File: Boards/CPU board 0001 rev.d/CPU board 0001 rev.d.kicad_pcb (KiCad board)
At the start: 2 copper layers, 165.9 x 187.4 mm, 78 parts, among them J1 CEC card edge connector large, U1 SPARE, U10 7432, U11 7442, U12 7406, U13 7406, U14 7442, U15 7442, U16 M8216, U17 M8216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

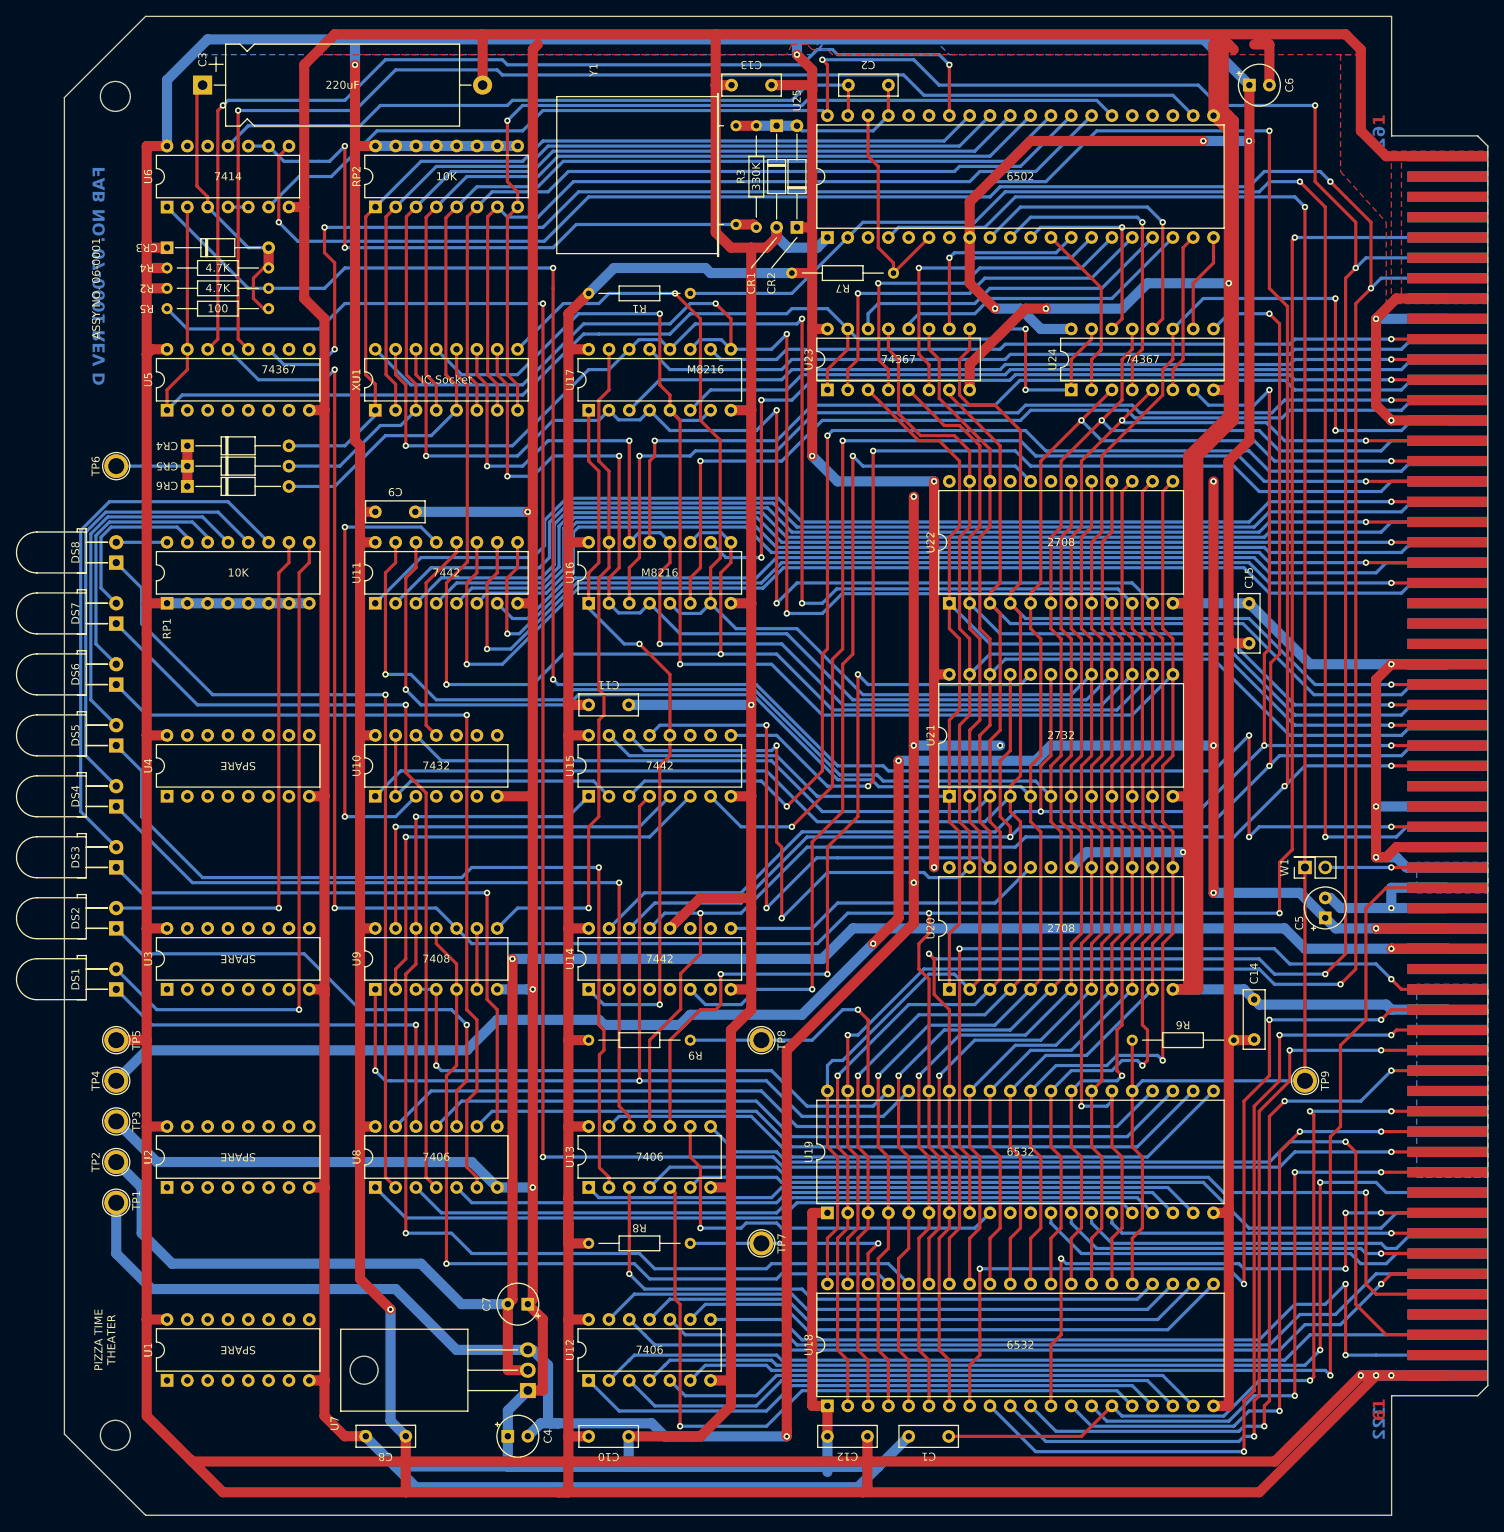
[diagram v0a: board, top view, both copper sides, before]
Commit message: updated boards per real one
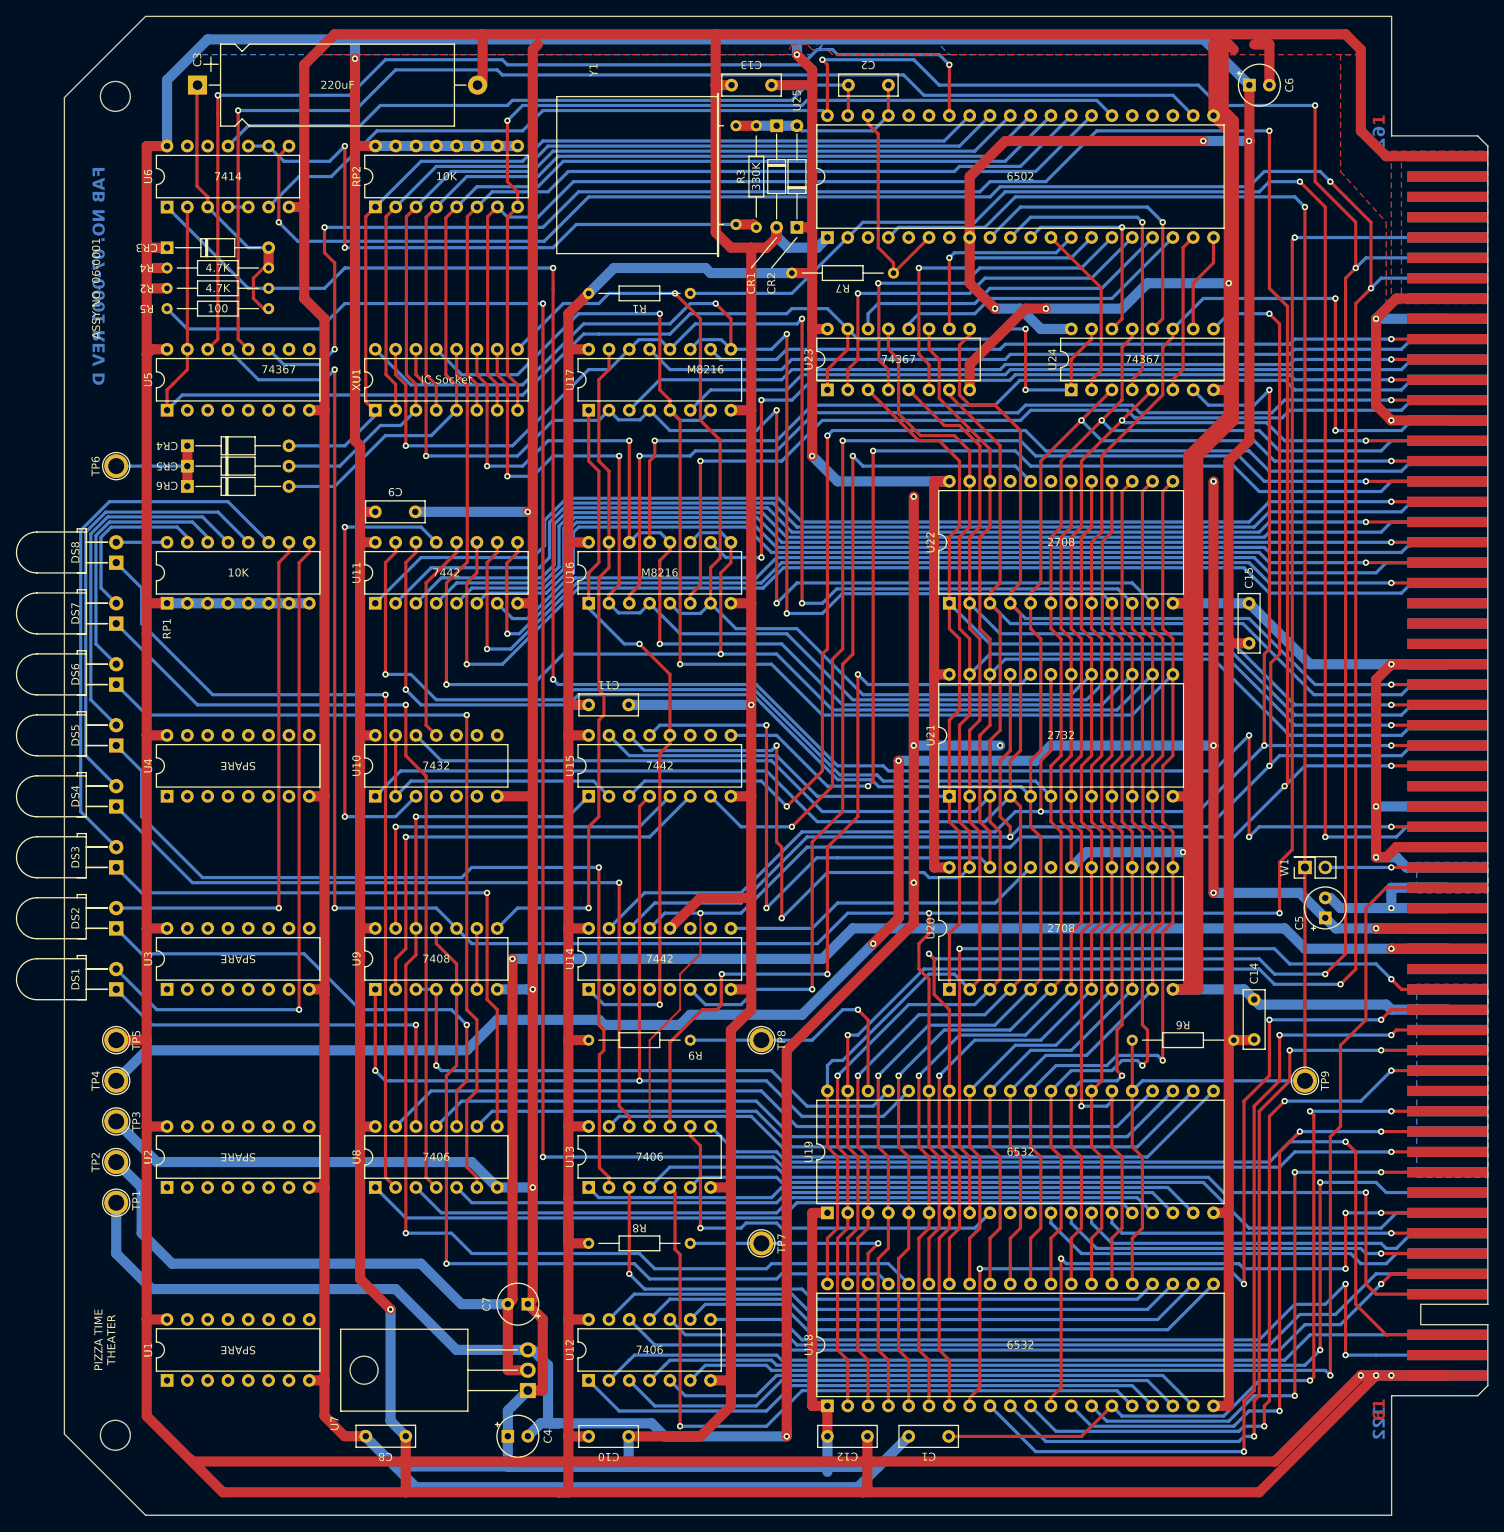
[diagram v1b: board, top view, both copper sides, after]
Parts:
- moved C3 0.63 mm to (58.4, 19.1)
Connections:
- U20 pad 24: unconnected-(U20-VCC-Pad24) -> +5V
- U22 pad 24: unconnected-(U22-VCC-Pad24) -> +5V
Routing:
- net +5V: track 1491.3 -> 1498.9 mm, vias 12 -> 10
- net cpu R/~{W}: track 132.6 -> 133.7 mm
- net Net-(CR3-A): track 35.8 -> 34.8 mm

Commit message: sent off boards for manufacture
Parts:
- U20, U22: value 2708 -> UNUSED
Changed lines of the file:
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@@
         (effects (font (size 1 1) (thickness 0.15)))
     )
-    (fp_text value "2708" (at 7.62 13.97 180) (layer "F.SilkS")
+    (fp_text value "UNUSED" (at 7.62 13.97 180) (layer "F.SilkS")
         (effects (font (size 1 1) (thickness 0.15)))
     )
@@
         (effects (font (size 1 1) (thickness 0.15)))
     )
-    (fp_text value "4.7K" (at 3.81 1.92) (layer "F.Fab")
+    (fp_text value "4.7K" (at 3.81 0) (layer "F.SilkS")
         (effects (font (size 1 1) (thickness 0.15)))
     )
@@
         (effects (font (size 1 1) (thickness 0.15)))
     )
-    (fp_text value "4.7K" (at 3.81 1.92) (layer "F.Fab")
+    (fp_text value "4.7K" (at 3.81 0) (layer "F.SilkS")
         (effects (font (size 1 1) (thickness 0.15)))
     )
@@
         (effects (font (size 1 1) (thickness 0.15)))
     )
-    (fp_text value "4.7K" (at 3.81 1.92) (layer "F.Fab")
+    (fp_text value "4.7K" (at 3.81 0) (layer "F.SilkS")
         (effects (font (size 1 1) (thickness 0.15)))
     )
@@
         (effects (font (size 1 1) (thickness 0.15)))
     )
-    (fp_text value "4.7K" (at 3.81 1.92) (layer "F.Fab")
+    (fp_text value "4.7K" (at 3.81 0) (layer "F.SilkS")
         (effects (font (size 1 1) (thickness 0.15)))
     )
@@
         (effects (font (size 1 1) (thickness 0.15)))
     )
-    (fp_text value "2708" (at 7.62 13.97 180) (layer "F.SilkS")
+    (fp_text value "UNUSED" (at 7.62 13.97 180) (layer "F.SilkS")
         (effects (font (size 1 1) (thickness 0.15)))
     )
@@
         (effects (font (size 1 1) (thickness 0.15)))
     )
-    (fp_text value "1Mhz" (at 17.16 4.6125) (layer "F.Fab")
+    (fp_text value "1Mhz" (at 5.715 12.065) (layer "F.SilkS")
         (effects (font (size 1 1) (thickness 0.15)))
     )
@@
         (effects (font (size 1 1) (thickness 0.15)))
     )
-    (fp_text value "4.7K" (at 3.81 1.92) (layer "F.Fab")
+    (fp_text value "4.7K" (at 3.81 0) (layer "F.SilkS")
         (effects (font (size 1 1) (thickness 0.15)))
     )

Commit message: revisions from real life boards
tip130a is actually tip30a, widened holes for crystal, widened holes for big power resistor, fixed cpu board LED resistors
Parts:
- RP1: value 10K -> 330
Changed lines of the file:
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@@
         (effects (font (size 1 1) (thickness 0.15)))
     )
-    (fp_text value "10K" (at 3.81 8.89 180) (layer "F.SilkS")
+    (fp_text value "330" (at 3.81 8.89 180) (layer "F.SilkS")
         (effects (font (size 1 1) (thickness 0.15)))
     )
@@
     (fp_line (start 16.135 2.5) (end -3.795 2.5)
       (stroke (width 0.1) (type solid)) (layer "F.Fab"))
-    (pad "1" thru_hole circle (at 0 0 270) (size 1.4 1.4) (drill 0.7) (layers "*.Cu" "*.Mask")
+    (pad "1" thru_hole circle (at 0 0 270) (size 2 2) (drill 1) (layers "*.Cu" "*.Mask")
       (net 8 "Net-(CR1-K)") (pinfunction "1") (pintype "passive"))
-    (pad "2" thru_hole circle (at 12.34 0 270) (size 1.4 1.4) (drill 0.7) (layers "*.Cu" "*.Mask")
+    (pad "2" thru_hole circle (at 12.34 0 270) (size 2 2) (drill 1) (layers "*.Cu" "*.Mask")
       (net 114 "Net-(R3-Pad1)") (pinfunction "2") (pintype "passive"))
     (model "${KICAD6_3DMODEL_DIR}/Crystal.3dshapes/Crystal_HC33-U_Horizontal.wrl"

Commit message: fixed rev.d pull up on CS and added render and schematic
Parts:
- added R10: 1K, Resistor_THT:R_Axial_DIN0309_L9.0mm_D3.2mm_P12.70mm_Horizontal, F.Cu at (151.1, 88.9)
- C1, C10, C11, C12, C13, C14, C15, C8, C9: footprint Capacitor_THT:C_Rect_L7.2mm_W2.5mm_P5.00mm_FKS2_FKP2_MKS2_MKP2 -> Capacitor_THT:C_Rect_L9.0mm_W2.5mm_P7.50mm_MKT
- CR1, CR2, CR3, CR4, CR5, CR6: footprint Diode_THT:D_DO-35_SOD27_P12.70mm_Horizontal -> Diode_THT:D_DO-35_SOD27_P7.62mm_Horizontal
- DS1, DS2, DS3, DS4, DS5, DS6, DS7, DS8: footprint Evan's parts:LED_D5.0mm_Horizontal_O3.81mm_Z15.0mm reversed -> LED_THT:LED_D5.0mm_Horizontal_O3.81mm_Z15.0mm
- R1, R2, R3, R4, R5, R6, R7, R8, R9: footprint Evan's parts:R_Axial_DIN0204_L3.6mm_D1.6mm_P12.7mm_Horizontal -> Resistor_THT:R_Axial_DIN0309_L9.0mm_D3.2mm_P12.70mm_Horizontal
- TP1, TP2, TP3, TP4, TP5, TP6, TP7, TP8, TP9: footprint TestPoint:TestPoint_Plated_Hole_D2.0mm -> TestPoint:TestPoint_Plated_Hole_D3.0mm
- U20, U22: value UNUSED -> 2708
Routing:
- net /CS 2732: track 97.7 -> 105.3 mm, vias 3 -> 2
